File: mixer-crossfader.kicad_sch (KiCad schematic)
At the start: 25 parts, among them U1601 TL072

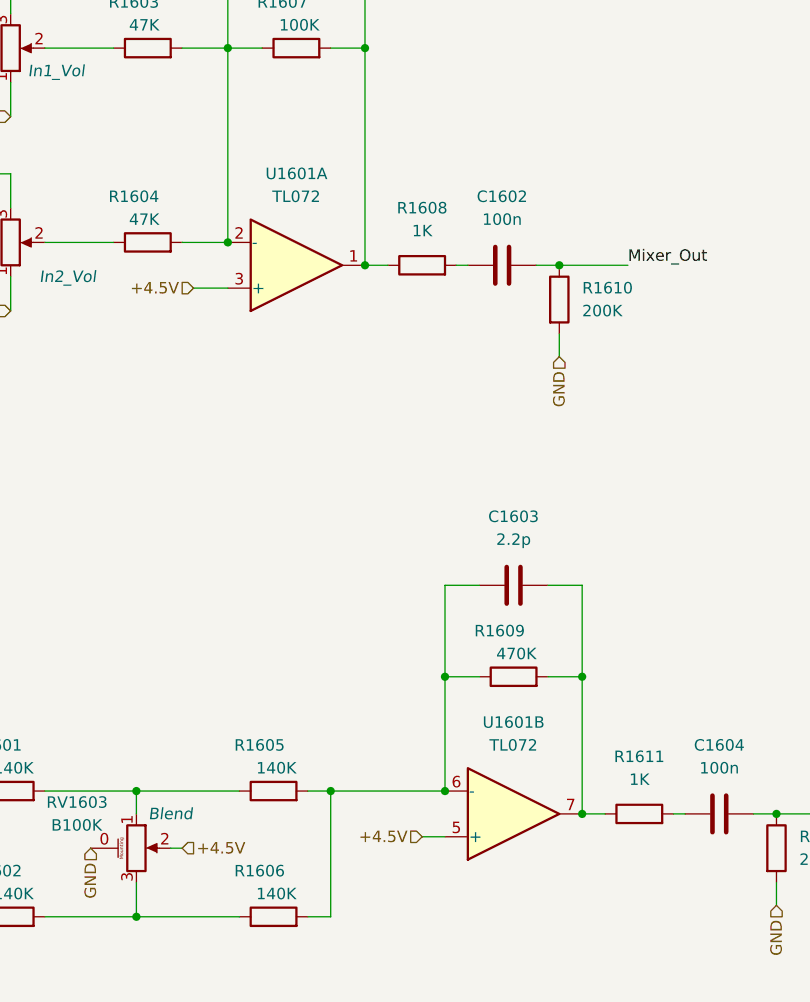
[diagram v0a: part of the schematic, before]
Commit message: Mixer/Crossfader layout done
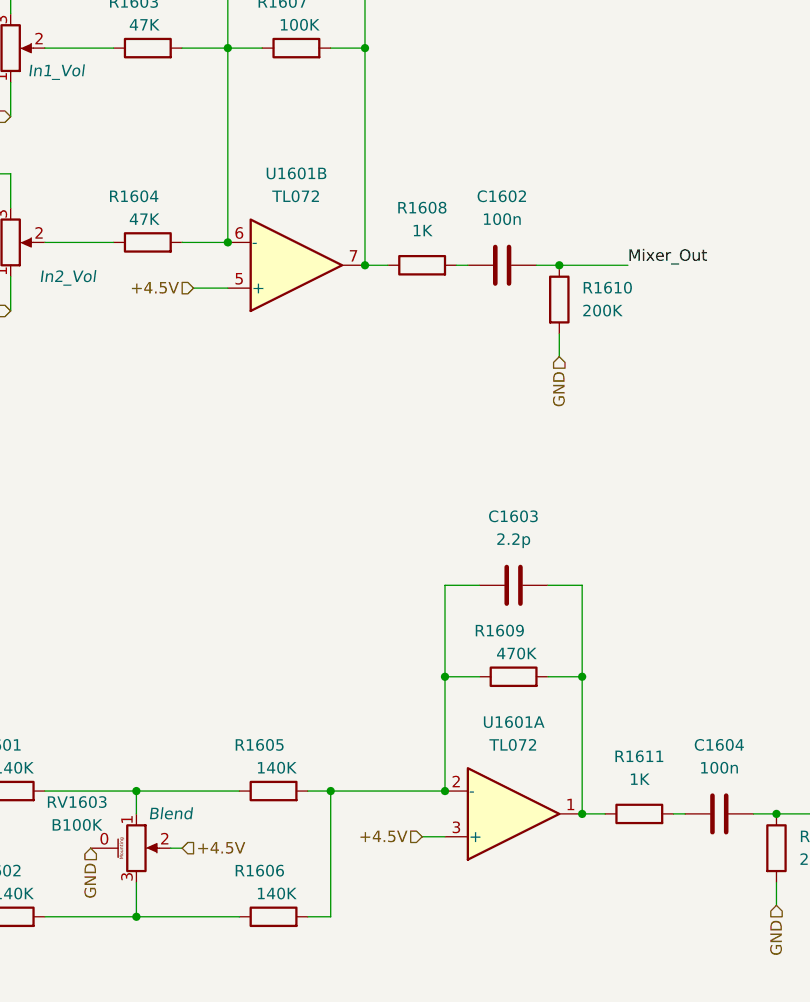
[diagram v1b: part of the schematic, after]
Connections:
- net +4.5V: now also U1601.3 (+), U1601.5 (+); no longer U1601.3 (+), U1601.5 (+)
- net at C1603.1, R1605.2, R1606.2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: now also U1601.2 (-); no longer U1601.6 (-)
- net at C1603.2, R1609.2, R1611.1: now also U1601.1; no longer U1601.7
- net at C1601.1, R1603.2, R1604.2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: now also U1601.6 (-); no longer U1601.2 (-)
- net at C1601.2, R1607.2, R1608.1: now also U1601.7; no longer U1601.1
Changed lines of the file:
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@@
     (pin "2")
   )
-  (symbol (lib_id "Amplifier_Operational:TL072") (at 114.3 119.38 0) (mirror x) (unit 2)
+  (symbol (lib_id "Amplifier_Operational:TL072") (at 114.3 119.38 0) (mirror x) (unit 1)
     (in_bom yes) (on_board yes) (fields_autoplaced)
     (property "Reference" "U1601" (id 0) (at 114.3 109.22 0))
@@
     (pin "2")
   )
-  (symbol (lib_id "Amplifier_Operational:TL072") (at 90.17 58.42 0) (mirror x) (unit 1)
+  (symbol (lib_id "Amplifier_Operational:TL072") (at 90.17 58.42 0) (mirror x) (unit 2)
     (in_bom yes) (on_board yes) (fields_autoplaced)
     (property "Reference" "U1601" (id 0) (at 90.17 48.26 0))

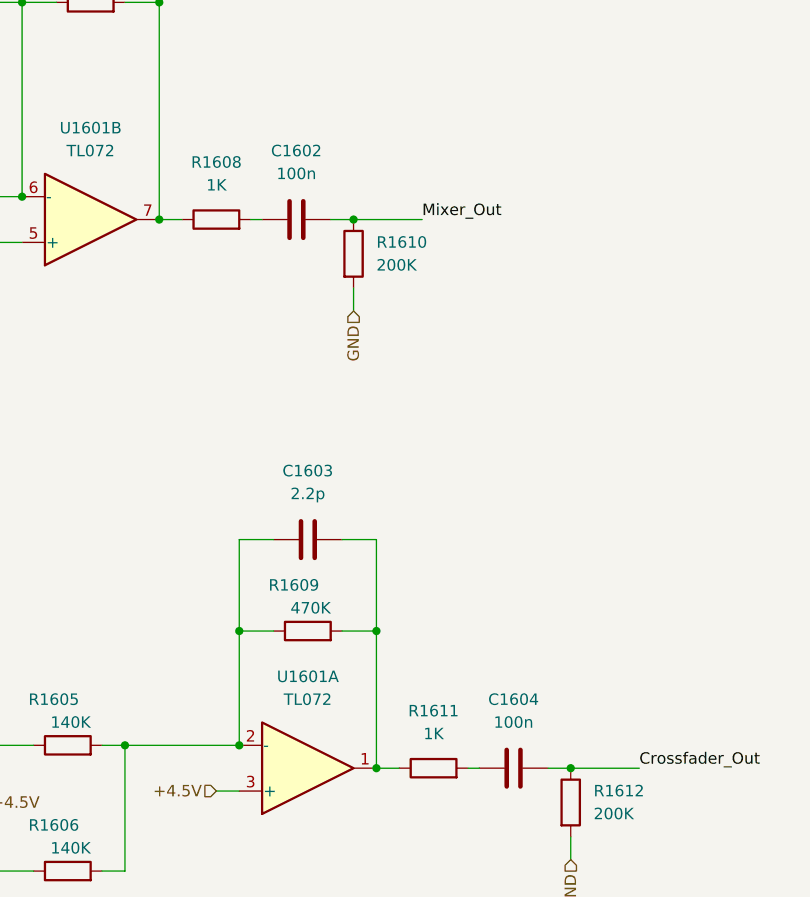
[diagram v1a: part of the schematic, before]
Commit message: Increase the size of dc blocking caps
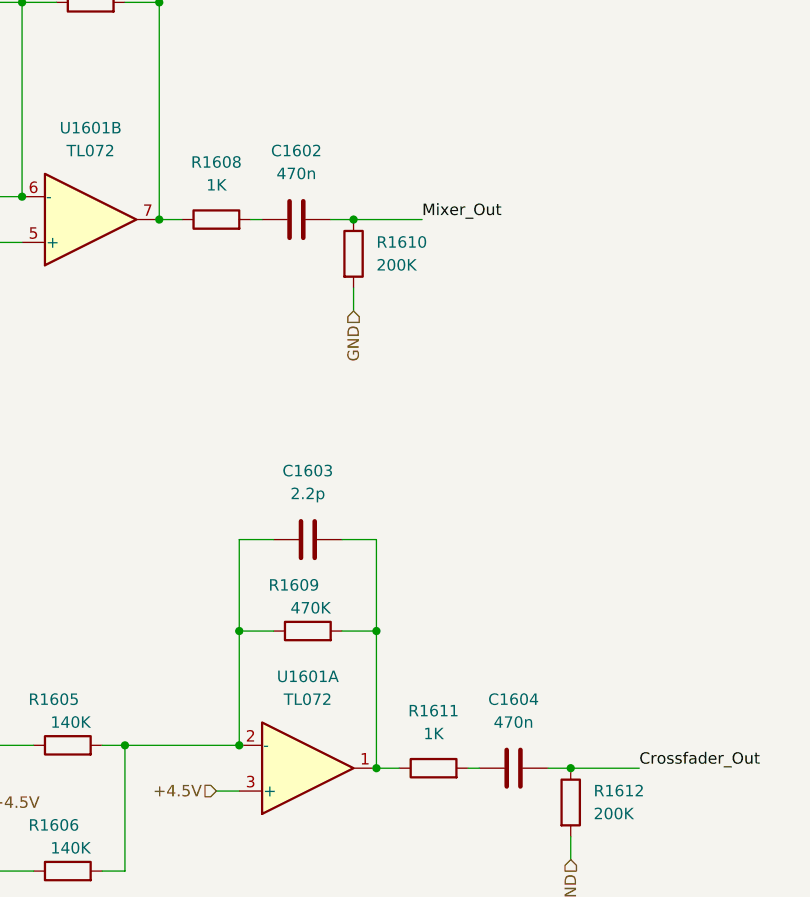
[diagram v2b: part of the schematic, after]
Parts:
- C1602, C1604: value 100n -> 470n; footprint Capacitor_SMD:C_0603_1608Metric_Pad1.08x0.95mm_HandSolder -> Capacitor_SMD:C_0805_2012Metric_Pad1.18x1.45mm_HandSolder
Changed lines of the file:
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@@
-    (pin "2")
-  )
-  (symbol (lib_id "Device:C") (at 113.03 58.42 90) (unit 1)
-    (in_bom yes) (on_board yes) (fields_autoplaced)
-    (property "Reference" "C1602" (id 0) (at 113.03 50.8 90))
-    (property "Value" "100n" (id 1) (at 113.03 53.34 90))
-    (property "Footprint" "Capacitor_SMD:C_0603_1608Metric_Pad1.08x0.95mm_HandSolder" (id 2) (at 116.84 57.4548 0)
-      (effects (font (size 1.27 1.27)) hide)
-    )
-    (property "Datasheet" "~" (id 3) (at 113.03 58.42 0)
-      (effects (font (size 1.27 1.27)) hide)
-    )
-    (pin "1")
     (pin "2")
   )
@@
     (pin "8")
   )
+  (symbol (lib_id "Device:C") (at 113.03 58.42 90) (unit 1)
+    (in_bom yes) (on_board yes) (fields_autoplaced)
+    (property "Reference" "C1602" (id 0) (at 113.03 50.8 90))
+    (property "Value" "470n" (id 1) (at 113.03 53.34 90))
+    (property "Footprint" "Capacitor_SMD:C_0805_2012Metric_Pad1.18x1.45mm_HandSolder" (id 2) (at 116.84 57.4548 0)
+      (effects (font (size 1.27 1.27)) hide)
+    )
+    (property "Datasheet" "~" (id 3) (at 113.03 58.42 0)
+      (effects (font (size 1.27 1.27)) hide)
+    )
+    (pin "1")
+    (pin "2")
+  )
   (symbol (lib_id "Device:R") (at 73.66 55.88 90) (unit 1)
     (in_bom yes) (on_board yes)
@@
     (pin "8")
   )
-  (symbol (lib_id "Device:C") (at 137.16 119.38 90) (unit 1)
-    (in_bom yes) (on_board yes) (fields_autoplaced)
-    (property "Reference" "C1604" (id 0) (at 137.16 111.76 90))
-    (property "Value" "100n" (id 1) (at 137.16 114.3 90))
-    (property "Footprint" "Capacitor_SMD:C_0603_1608Metric_Pad1.08x0.95mm_HandSolder" (id 2) (at 140.97 118.4148 0)
-      (effects (font (size 1.27 1.27)) hide)
-    )
-    (property "Datasheet" "~" (id 3) (at 137.16 119.38 0)
-      (effects (font (size 1.27 1.27)) hide)
-    )
-    (pin "1")
-    (pin "2")
-  )
   (symbol (lib_id "R0904NB10KL-25KQ:R_Potentiometer_Shield") (at 72.39 123.19 0) (unit 1)
     (in_bom yes) (on_board yes)
@@
       (effects (font (size 1.27 1.27)) hide)
     )
+    (pin "1")
+    (pin "2")
+  )
+  (symbol (lib_id "Device:C") (at 137.16 119.38 90) (unit 1)
+    (in_bom yes) (on_board yes) (fields_autoplaced)
+    (property "Reference" "C1604" (id 0) (at 137.16 111.76 90))
+    (property "Value" "470n" (id 1) (at 137.16 114.3 90))
+    (property "Footprint" "Capacitor_SMD:C_0805_2012Metric_Pad1.18x1.45mm_HandSolder" (id 2) (at 140.97 118.4148 0)
+      (effects (font (size 1.27 1.27)) hide)
+    )
+    (property "Datasheet" "~" (id 3) (at 137.16 119.38 0)
+      (effects (font (size 1.27 1.27)) hide)
+    )

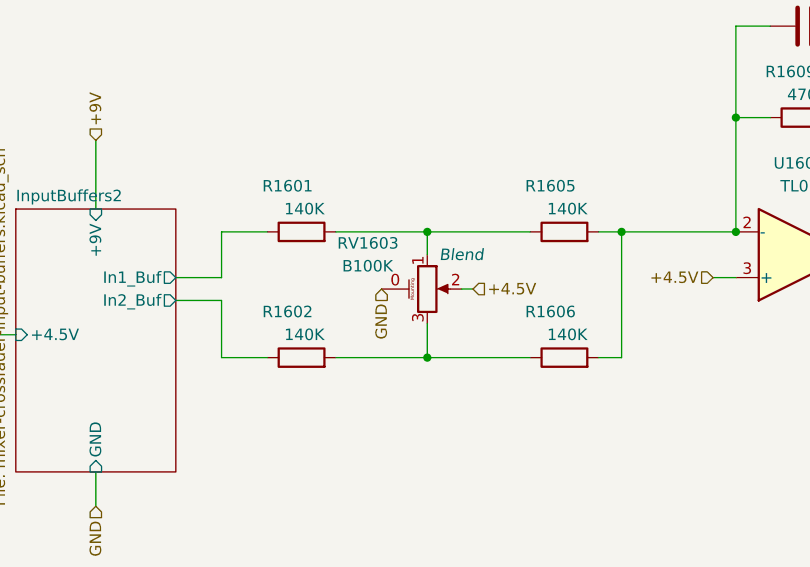
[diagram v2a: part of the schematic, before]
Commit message: Fix: crossfader pot orientation
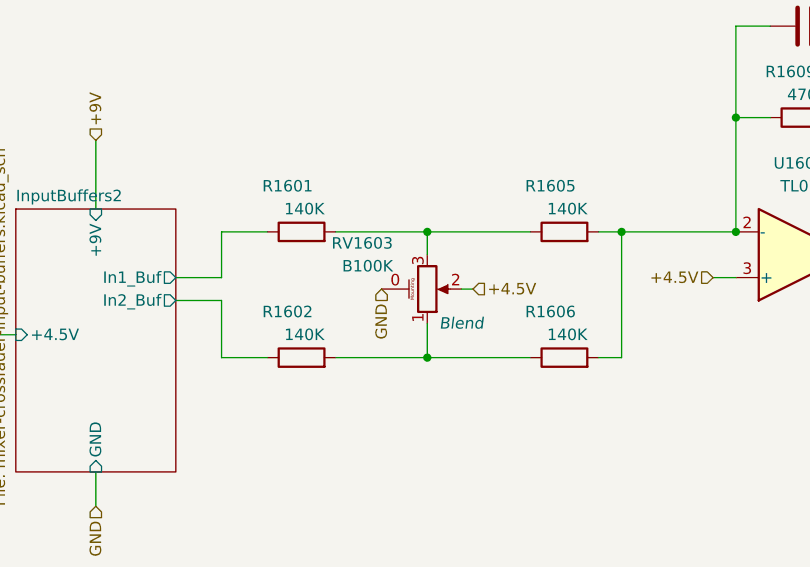
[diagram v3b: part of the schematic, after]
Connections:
- net at R1601.2, R1605.1: now also RV1603.3; no longer RV1603.1
- net at R1602.2, R1606.1: now also RV1603.1; no longer RV1603.3
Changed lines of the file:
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@@
     (pin "8")
   )
-  (symbol (lib_id "R0904NB10KL-25KQ:R_Potentiometer_Shield") (at 72.39 123.19 0) (unit 1)
+  (symbol (lib_id "R0904NB10KL-25KQ:R_Potentiometer_Shield") (at 72.39 123.19 0) (mirror x) (unit 1)
     (in_bom yes) (on_board yes)
-    (property "Reference" "RV1603" (id 0) (at 69.215 118.11 0)
+    (property "Reference" "RV1603" (id 0) (at 68.58 118.11 0)
       (effects (font (size 1.27 1.27)) (justify right))
     )
@@
       (effects (font (size 1.27 1.27)) hide)
     )
-    (property "Role" "Blend" (id 4) (at 76.2 119.38 0)
+    (property "Role" "Blend" (id 4) (at 76.2 127 0)
       (effects (font (size 1.27 1.27) italic))
     )

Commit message: Add JLC parts numbers
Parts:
- C1601: LCSC (none) -> C91367; Role (none) -> opamp-filter
- C1602, C1604: LCSC (none) -> C651004; Role (none) -> audio-coupling
- C1603: LCSC (none) -> C1651; Role (none) -> audio-filter
- C1605: LCSC (none) -> C497032; Role (none) -> ic-bypass
- D1601, D1602: LCSC (none) -> C20936
- R1601, R1602, R1605, R1606: LCSC (none) -> C321721
- R1603, R1604: LCSC (none) -> C111134
- R1607: LCSC (none) -> C14675
- R1608, R1611: LCSC (none) -> C2907002
- R1609: LCSC (none) -> C2907040
- R1610, R1612: LCSC (none) -> C203392
- U1601: LCSC (none) -> C67473
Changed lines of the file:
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@@
+      (effects (font (size 1.27 1.27)) hide)
+    )
+    (property "LCSC" "C321721" (id 4) (at 58.42 116.84 0)
       (effects (font (size 1.27 1.27)) hide)
     )
@@
       (effects (font (size 1.27 1.27)) hide)
     )
+    (property "LCSC" "C20936" (id 4) (at 38.1 177.8 0)
+      (effects (font (size 1.27 1.27)) hide)
+    )
     (pin "1")
     (pin "2")
@@
       (effects (font (size 1.27 1.27)) hide)
     )
+    (property "LCSC" "C203392" (id 4) (at 143.51 123.19 0)
+      (effects (font (size 1.27 1.27)) hide)
+    )
     (pin "1")
     (pin "2")
@@
     )
     (property "Datasheet" "~" (id 3) (at 114.3 104.14 0)
+      (effects (font (size 1.27 1.27)) hide)
+    )
+    (property "LCSC" "C2907040" (id 4) (at 114.3 104.14 0)
       (effects (font (size 1.27 1.27)) hide)
     )
@@
     )
     (property "Datasheet" "~" (id 3) (at 85.09 177.8 0)
+      (effects (font (size 1.27 1.27)) hide)
+    )
+    (property "LCSC" "C20936" (id 4) (at 85.09 177.8 0)
       (effects (font (size 1.27 1.27)) hide)
     )
@@
       (effects (font (size 1.27 1.27)) hide)
     )
+    (property "LCSC" "C2907002" (id 4) (at 128.27 119.38 0)
+      (effects (font (size 1.27 1.27)) hide)
+    )
     (pin "1")
     (pin "2")
@@
     )
     (property "Datasheet" "http://www.ti.com/lit/ds/symlink/tl071.pdf" (id 3) (at 114.3 119.38 0)
+      (effects (font (size 1.27 1.27)) hide)
+    )
+    (property "LCSC" "C67473" (id 4) (at 114.3 119.38 0)
       (effects (font (size 1.27 1.27)) hide)
     )
@@
       (effects (font (size 1.27 1.27)) hide)
     )
+    (property "LCSC" "C651004" (id 4) (at 113.03 58.42 0)
+      (effects (font (size 1.27 1.27)) hide)
+    )
+    (property "Role" "audio-coupling" (id 5) (at 113.03 58.42 0)
+      (effects (font (size 1.27 1.27)) hide)
+    )
     (pin "1")
     (pin "2")
@@
     )
     (property "Datasheet" "~" (id 3) (at 73.66 55.88 0)
+      (effects (font (size 1.27 1.27)) hide)
+    )
+    (property "LCSC" "C111134" (id 4) (at 73.66 55.88 0)
       (effects (font (size 1.27 1.27)) hide)
     )
@@
       (effects (font (size 1.27 1.27)) hide)
     )
+    (property "LCSC" "C1651" (id 4) (at 114.3 93.98 0)
+      (effects (font (size 1.27 1.27)) hide)
+    )
+    (property "Role" "audio-filter" (id 5) (at 114.3 93.98 0)
+      (effects (font (size 1.27 1.27)) hide)
+    )
     (pin "1")
     (pin "2")
@@
     )
     (property "Datasheet" "~" (id 3) (at 87.63 130.81 0)
+      (effects (font (size 1.27 1.27)) hide)
+    )
+    (property "LCSC" "C321721" (id 4) (at 87.63 130.81 0)
       (effects (font (size 1.27 1.27)) hide)
     )
@@
     )
     (property "Datasheet" "http://www.ti.com/lit/ds/symlink/tl071.pdf" (id 3) (at 90.17 58.42 0)
+      (effects (font (size 1.27 1.27)) hide)
+    )
+    (property "LCSC" "C67473" (id 4) (at 90.17 58.42 0)
       (effects (font (size 1.27 1.27)) hide)
     )
@@
       (effects (font (size 1.27 1.27)) hide)
     )
+    (property "LCSC" "C14675" (id 4) (at 90.17 34.29 0)
+      (effects (font (size 1.27 1.27)) hide)
+    )
     (pin "1")
     (pin "2")
@@
       (effects (font (size 1.27 1.27)) hide)
     )
+    (property "LCSC" "C111134" (id 4) (at 73.66 34.29 0)
+      (effects (font (size 1.27 1.27)) hide)
+    )
     (pin "1")
     (pin "2")
@@
       (effects (font (size 1.27 1.27)) hide)
     )
+    (property "LCSC" "C203392" (id 4) (at 119.38 62.23 0)
+      (effects (font (size 1.27 1.27)) hide)
+    )
     (pin "1")
     (pin "2")
@@
       (effects (font (size 1.27 1.27)) hide)
     )
+    (property "LCSC" "C497032" (id 4) (at 243.84 45.72 0)
+      (effects (font (size 1.27 1.27)) hide)
+    )
+    (property "Role" "ic-bypass" (id 5) (at 243.84 45.72 0)
+      (effects (font (size 1.27 1.27)) hide)
+    )
     (pin "1")
     (pin "2")
@@
     )
     (property "Datasheet" "~" (id 3) (at 58.42 130.81 0)
+      (effects (font (size 1.27 1.27)) hide)
+    )
+    (property "LCSC" "C321721" (id 4) (at 58.42 130.81 0)
       (effects (font (size 1.27 1.27)) hide)
     )
@@
       (effects (font (size 1.27 1.27)) hide)
     )
+    (property "LCSC" "C2907002" (id 4) (at 104.14 58.42 0)
+      (effects (font (size 1.27 1.27)) hide)
+    )
     (pin "1")
     (pin "2")
@@
     )
     (property "Datasheet" "~" (id 3) (at 87.63 116.84 0)
+      (effects (font (size 1.27 1.27)) hide)
+    )
+    (property "LCSC" "C321721" (id 4) (at 87.63 116.84 0)
       (effects (font (size 1.27 1.27)) hide)
     )
@@
       (effects (font (size 1.27 1.27)) hide)
     )
+    (property "LCSC" "C91367" (id 4) (at 90.17 22.86 0)
+      (effects (font (size 1.27 1.27)) hide)
+    )
+    (property "Role" "opamp-filter" (id 5) (at 90.17 22.86 0)
+      (effects (font (size 1.27 1.27)) hide)
+    )
     (pin "1")
     (pin "2")
@@
       (effects (font (size 1.27 1.27)) hide)
     )
+    (property "LCSC" "C651004" (id 4) (at 137.16 119.38 0)
+      (effects (font (size 1.27 1.27)) hide)
+    )
+    (property "Role" "audio-coupling" (id 5) (at 137.16 119.38 0)
+      (effects (font (size 1.27 1.27)) hide)
+    )
     (pin "1")
     (pin "2")
@@
       (effects (font (size 1.27 1.27)) hide)
     )
+    (property "LCSC" "C67473" (id 4) (at 257.81 45.72 0)
+      (effects (font (size 1.27 1.27)) hide)
+    )
